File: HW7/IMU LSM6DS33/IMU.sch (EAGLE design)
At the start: 29 parts, among them J1 USB-MB-H

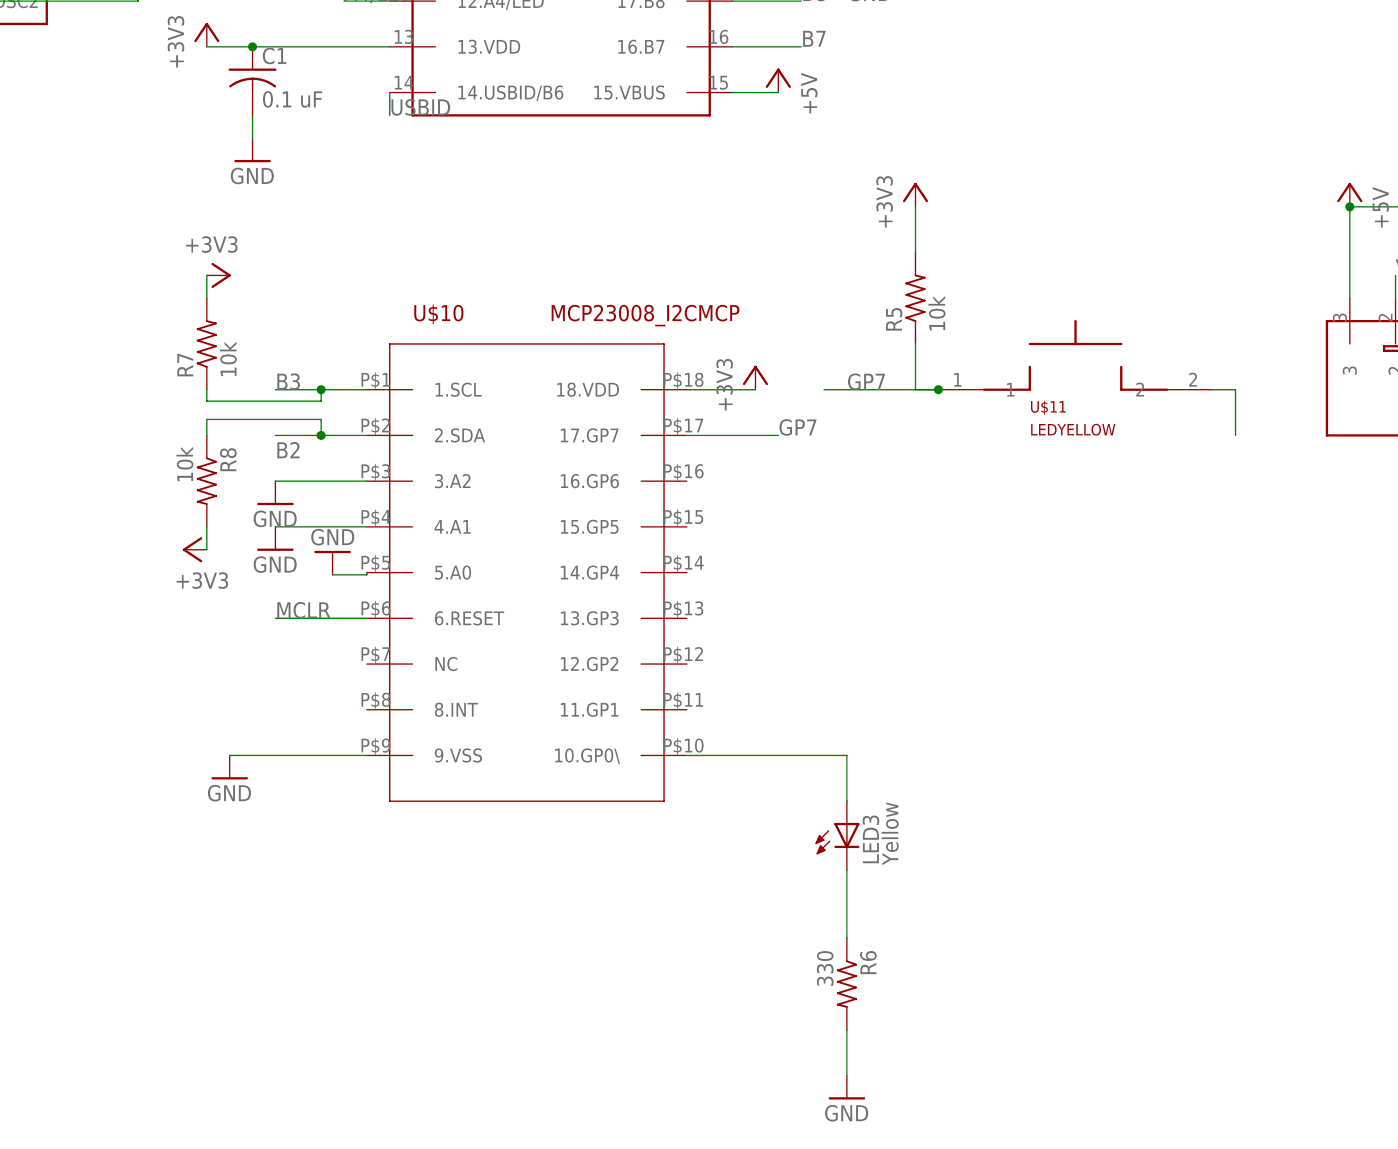
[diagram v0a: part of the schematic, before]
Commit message: Schematic for the IMU
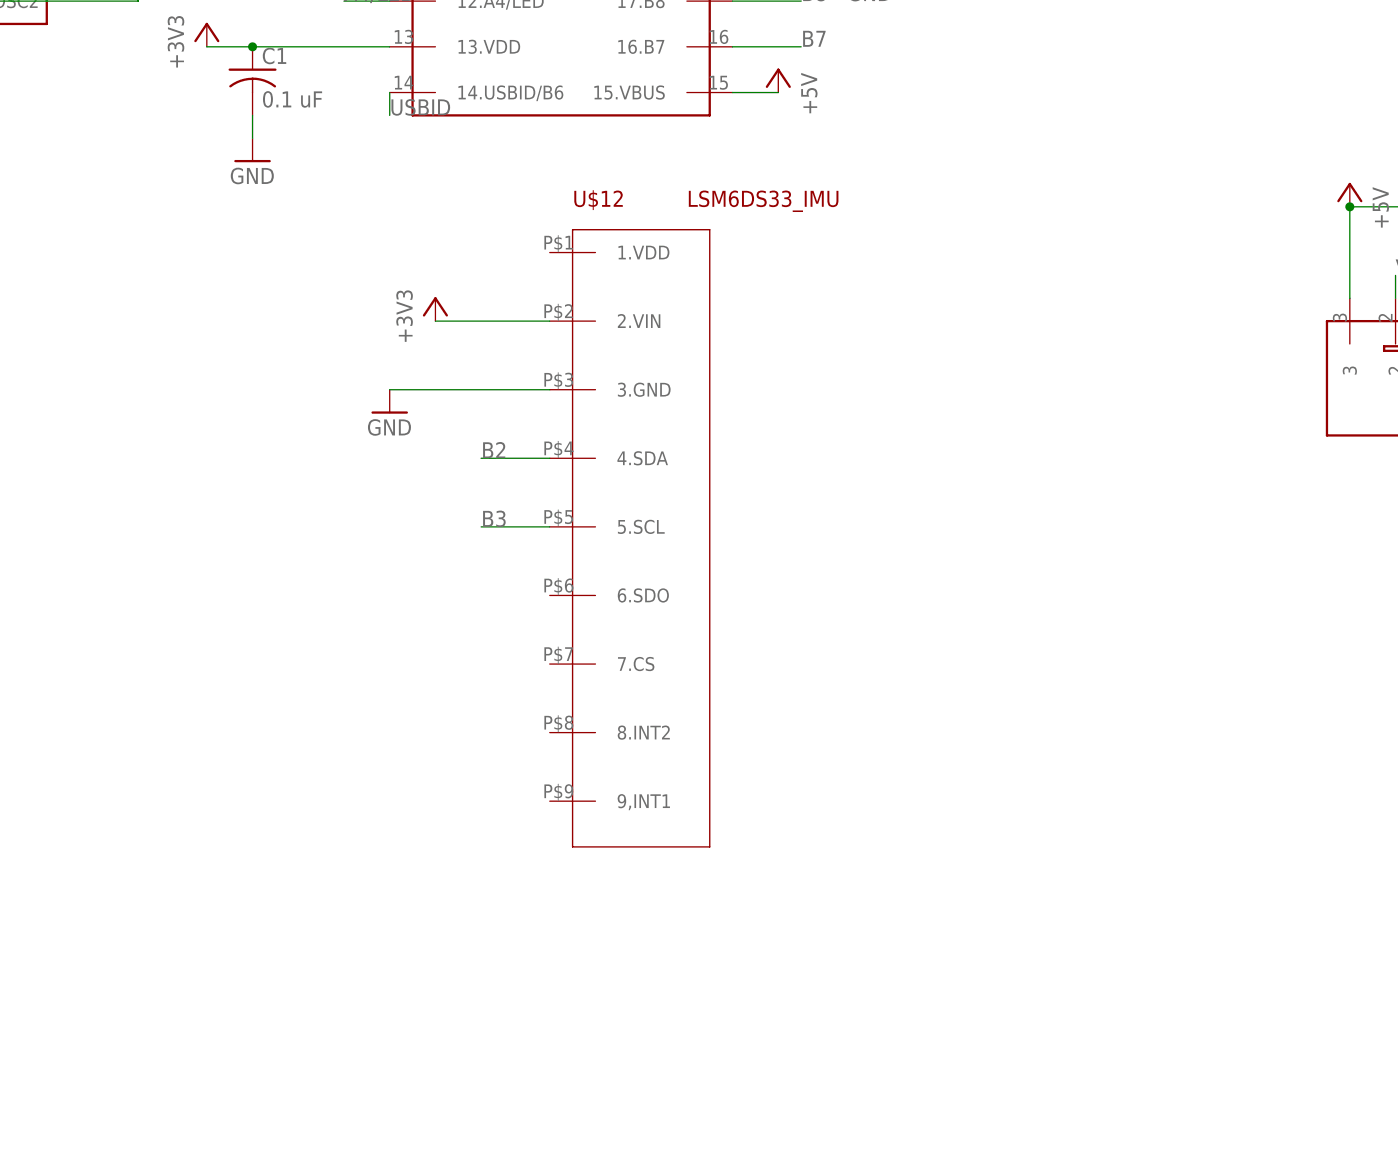
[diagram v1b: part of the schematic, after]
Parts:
- removed LED3: Yellow, led:LED3MM
- removed R5, R7, R8: 10k, 433:R-US_0207/10
- removed R6: 330, 433:R-US_0207/10
- removed U$10: MCP23008_I2CMCP, gen433:MCP23008_I2CMCP
- removed U$11: LEDYELLOW, 433:PB
- added U$12: LSM6DS33_IMU, gen433:LSM6DS33_IMU
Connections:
- removed net GND1: U$11.2
- removed net GP7: R5.1, U$10.17.GP7, U$11.1
- removed net N$10: LED3.C, R6.1
- net +3V3: now also U$12.2.VIN; no longer R5.2, R7.2, R8.2, U$10.18.VDD
- net A4/LED: no longer LED3.A, U$10.10.GP0\
- net B2: now also U$12.4.SDA; no longer R8.1, U$10.2.SDA
- net B3: now also U$12.5.SCL; no longer R7.1, U$10.1.SCL
- net GND: now also U$12.3.GND; no longer R6.2, U$10.3.A2, U$10.4.A1, U$10.5.A0, U$10.9.VSS
- net MCLR: no longer U$10.6.RESET
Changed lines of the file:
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@@
 <part name="P+3" library="433" deviceset="+5V" device=""/>
 <part name="+3V8" library="433" deviceset="+3V3" device=""/>
-<part name="U$10" library="gen433" deviceset="MCP23008_I2C" device="MCP"/>
-<part name="U$11" library="433" deviceset="PB" device="" value="LEDYELLOW"/>
-<part name="R5" library="433" deviceset="R-US_" device="0207/10" package3d_urn="urn:adsk.eagle:package:25939/1" value="10k"/>
-<part name="+3V9" library="433" deviceset="+3V3" device=""/>
-<part name="+3V10" library="433" deviceset="+3V3" device=""/>
-<part name="LED3" library="led" library_urn="urn:adsk.eagle:library:259" deviceset="LED" device="3MM" package3d_urn="urn:adsk.eagle:package:15797/1" value="Yellow"/>
-<part name="R6" library="433" deviceset="R-US_" device="0207/10" package3d_urn="urn:adsk.eagle:package:25939/1" value="330"/>
-<part name="GND20" library="433" deviceset="GND" device=""/>
-<part name="GND21" library="433" deviceset="GND" device=""/>
-<part name="R7" library="433" deviceset="R-US_" device="0207/10" package3d_urn="urn:adsk.eagle:package:25939/1" value="10k"/>
-<part name="R8" library="433" deviceset="R-US_" device="0207/10" package3d_urn="urn:adsk.eagle:package:25939/1" value="10k"/>
-<part name="+3V11" library="433" deviceset="+3V3" device=""/>
-<part name="+3V12" library="433" deviceset="+3V3" device=""/>
-<part name="GND22" library="433" deviceset="GND" device=""/>
-<part name="GND23" library="433" deviceset="GND" device=""/>
-<part name="GND24" library="433" deviceset="GND" device=""/>
+<part name="U$12" library="gen433" deviceset="LSM6DS33_IMU" device=""/>
+<part name="+3V13" library="gen433" deviceset="+3V3" device=""/>
+<part name="GND25" library="gen433" deviceset="GND" device=""/>
 </parts>
 <sheets>
@@
 <instance part="P+3" gate="1" x="236.22" y="121.92"/>
 <instance part="+3V8" gate="G$1" x="91.44" y="55.88"/>
-<instance part="U$10" gate="G$1" x="50.8" y="-35.56"/>
-<instance part="U$11" gate="G$1" x="106.68" y="-20.32"/>
-<instance part="R5" gate="G$1" x="88.9" y="-10.16" rot="R90"/>
-<instance part="+3V9" gate="G$1" x="88.9" y="2.54"/>
-<instance part="+3V10" gate="G$1" x="71.12" y="-17.78"/>
-<instance part="LED3" gate="G$1" x="81.28" y="-68.58"/>
-<instance part="R6" gate="G$1" x="81.28" y="-86.36" rot="R270"/>
-<instance part="GND20" gate="1" x="81.28" y="-99.06"/>
-<instance part="GND21" gate="1" x="12.7" y="-63.5"/>
-<instance part="R7" gate="G$1" x="10.16" y="-15.24" rot="R90"/>
-<instance part="R8" gate="G$1" x="10.16" y="-30.48" rot="R270"/>
-<instance part="+3V11" gate="G$1" x="12.7" y="-7.62" rot="R270"/>
-<instance part="+3V12" gate="G$1" x="7.62" y="-38.1" rot="R90"/>
-<instance part="GND22" gate="1" x="17.78" y="-33.02"/>
-<instance part="GND23" gate="1" x="17.78" y="-38.1"/>
-<instance part="GND24" gate="1" x="24.13" y="-38.354" rot="R180"/>
+<instance part="U$12" gate="G$1" x="73.66" y="-27.94"/>
+<instance part="+3V13" gate="G$1" x="35.56" y="-10.16"/>
+<instance part="GND25" gate="1" x="30.48" y="-22.86"/>
 </instances>
 <busses>
@@
 </segment>
 <segment>
-<pinref part="GND20" gate="1" pin="GND"/>
-<pinref part="R6" gate="G$1" pin="2"/>
-<wire x1="81.28" y1="-96.52" x2="81.28" y2="-91.44" width="0.1524" layer="91"/>
-</segment>
-<segment>
-<pinref part="U$10" gate="G$1" pin="9.VSS"/>
-<wire x1="27.94" y1="-60.96" x2="12.7" y2="-60.96" width="0.1524" layer="91"/>
-<pinref part="GND21" gate="1" pin="GND"/>
-</segment>
-<segment>
-<pinref part="U$10" gate="G$1" pin="4.A1"/>
-<pinref part="GND23" gate="1" pin="GND"/>
-<wire x1="27.94" y1="-35.56" x2="17.78" y2="-35.56" width="0.1524" layer="91"/>
-</segment>
-<segment>
-<pinref part="U$10" gate="G$1" pin="3.A2"/>
-<pinref part="GND22" gate="1" pin="GND"/>
-<wire x1="27.94" y1="-30.48" x2="17.78" y2="-30.48" width="0.1524" layer="91"/>
-</segment>
-<segment>
-<pinref part="U$10" gate="G$1" pin="5.A0"/>
-<pinref part="GND24" gate="1" pin="GND"/>
-<wire x1="27.94" y1="-40.64" x2="27.94" y2="-40.894" width="0.1524" layer="91"/>
-<wire x1="27.94" y1="-40.894" x2="24.13" y2="-40.894" width="0.1524" layer="91"/>
+<pinref part="U$12" gate="G$1" pin="3.GND"/>
+<pinref part="GND25" gate="1" pin="GND"/>
+<wire x1="48.26" y1="-20.32" x2="30.48" y2="-20.32" width="0.1524" layer="91"/>
 </segment>
 </net>
@@
 </segment>
 <segment>
-<pinref part="R5" gate="G$1" pin="2"/>
-<pinref part="+3V9" gate="G$1" pin="+3V3"/>
-<wire x1="88.9" y1="-5.08" x2="88.9" y2="0" width="0.1524" layer="91"/>
-</segment>
-<segment>
-<pinref part="U$10" gate="G$1" pin="18.VDD"/>
-<pinref part="+3V10" gate="G$1" pin="+3V3"/>
-<wire x1="63.5" y1="-20.32" x2="71.12" y2="-20.32" width="0.1524" layer="91"/>
-</segment>
-<segment>
-<pinref part="R8" gate="G$1" pin="2"/>
-<pinref part="+3V12" gate="G$1" pin="+3V3"/>
-<wire x1="10.16" y1="-35.56" x2="10.16" y2="-38.1" width="0.1524" layer="91"/>
-</segment>
-<segment>
-<pinref part="R7" gate="G$1" pin="2"/>
-<pinref part="+3V11" gate="G$1" pin="+3V3"/>
-<wire x1="10.16" y1="-10.16" x2="10.16" y2="-7.62" width="0.1524" layer="91"/>
+<pinref part="U$12" gate="G$1" pin="2.VIN"/>
+<wire x1="48.26" y1="-12.7" x2="35.56" y2="-12.7" width="0.1524" layer="91"/>
+<pinref part="+3V13" gate="G$1" pin="+3V3"/>
 </segment>
 </net>
@@
 <label x="215.9" y="78.74" size="1.778" layer="95"/>
 </segment>
-<segment>
-<pinref part="U$10" gate="G$1" pin="6.RESET"/>
-<wire x1="27.94" y1="-45.72" x2="17.78" y2="-45.72" width="0.1524" layer="91"/>
-<label x="17.78" y="-45.72" size="1.778" layer="95"/>
-</segment>
 </net>
 <net name="A0" class="0">
@@
 </segment>
 <segment>
-<pinref part="U$10" gate="G$1" pin="2.SDA"/>
-<label x="17.78" y="-27.94" size="1.778" layer="95"/>
-<wire x1="27.94" y1="-25.4" x2="22.86" y2="-25.4" width="0.1524" layer="91"/>
-<wire x1="22.86" y1="-25.4" x2="17.78" y2="-25.4" width="0.1524" layer="91"/>
-<wire x1="22.86" y1="-25.4" x2="22.86" y2="-23.622" width="0.1524" layer="91"/>
-<junction x="22.86" y="-25.4"/>
-<wire x1="22.86" y1="-23.622" x2="10.16" y2="-23.622" width="0.1524" layer="91"/>
-<pinref part="R8" gate="G$1" pin="1"/>
-<wire x1="10.16" y1="-23.622" x2="10.16" y2="-25.4" width="0.1524" layer="91"/>
+<pinref part="U$12" gate="G$1" pin="4.SDA"/>
+<wire x1="48.26" y1="-27.94" x2="40.64" y2="-27.94" width="0.1524" layer="91"/>
+<label x="40.64" y="-27.94" size="1.778" layer="95"/>
 </segment>
 </net>
@@
 </segment>
 <segment>
-<pinref part="U$10" gate="G$1" pin="1.SCL"/>
-<wire x1="27.94" y1="-20.32" x2="22.86" y2="-20.32" width="0.1524" layer="91"/>
-<label x="17.78" y="-20.32" size="1.778" layer="95"/>
-<wire x1="22.86" y1="-20.32" x2="17.78" y2="-20.32" width="0.1524" layer="91"/>
-<junction x="22.86" y="-20.32"/>
-<wire x1="22.86" y1="-20.32" x2="22.86" y2="-21.59" width="0.1524" layer="91"/>
-<wire x1="22.86" y1="-21.59" x2="10.16" y2="-21.59" width="0.1524" layer="91"/>
-<pinref part="R7" gate="G$1" pin="1"/>
-<wire x1="10.16" y1="-20.32" x2="10.16" y2="-21.59" width="0.1524" layer="91"/>
+<pinref part="U$12" gate="G$1" pin="5.SCL"/>
+<wire x1="48.26" y1="-35.56" x2="40.64" y2="-35.56" width="0.1524" layer="91"/>
+<label x="40.64" y="-35.56" size="1.778" layer="95"/>
 </segment>
 </net>
@@
 <label x="195.58" y="121.92" size="1.778" layer="95" rot="MR0"/>
 </segment>
-<segment>
-<pinref part="LED3" gate="G$1" pin="A"/>
-<wire x1="81.28" y1="-66.04" x2="81.28" y2="-60.96" width="0.1524" layer="91"/>
-<pinref part="U$10" gate="G$1" pin="10.GP0\"/>
-<wire x1="81.28" y1="-60.96" x2="63.5" y2="-60.96" width="0.1524" layer="91"/>
-</segment>
 </net>
 <net name="USBID" class="0">
@@
 </segment>
 </net>
-<net name="GND1" class="0">
-<segment>
-<pinref part="U$11" gate="G$1" pin="2"/>
-<wire x1="121.92" y1="-20.32" x2="124.46" y2="-20.32" width="0.1524" layer="91"/>
-<wire x1="124.46" y1="-20.32" x2="124.46" y2="-25.4" width="0.1524" layer="91"/>
-</segment>
-</net>
-<net name="GP7" class="0">
-<segment>
-<pinref part="U$11" gate="G$1" pin="1"/>
-<wire x1="91.44" y1="-20.32" x2="88.9" y2="-20.32" width="0.1524" layer="91"/>
-<pinref part="R5" gate="G$1" pin="1"/>
-<wire x1="88.9" y1="-20.32" x2="88.9" y2="-15.24" width="0.1524" layer="91"/>
-<wire x1="91.44" y1="-20.32" x2="78.74" y2="-20.32" width="0.1524" layer="91"/>
-<junction x="91.44" y="-20.32"/>
-<label x="81.28" y="-20.32" size="1.778" layer="95"/>
-</segment>
-<segment>
-<pinref part="U$10" gate="G$1" pin="17.GP7"/>
-<wire x1="63.5" y1="-25.4" x2="73.66" y2="-25.4" width="0.1524" layer="91"/>
-<label x="73.66" y="-25.4" size="1.778" layer="95"/>
-</segment>
-</net>
-<net name="N$10" class="0">
-<segment>
-<pinref part="R6" gate="G$1" pin="1"/>
-<pinref part="LED3" gate="G$1" pin="C"/>
-<wire x1="81.28" y1="-81.28" x2="81.28" y2="-73.66" width="0.1524" layer="91"/>
-</segment>
-</net>
